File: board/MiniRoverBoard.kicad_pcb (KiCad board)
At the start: 2 copper layers, 103.4 x 66.5 mm, 49 parts, among them J1 DEBUG, Q1 NMOS, Q2 BSS138, U2 OKI, U3 Opamp_Dual, U4 LT1910, U7 ESP32-S2-DEVKITM-1U, U8 Opamp_Dual

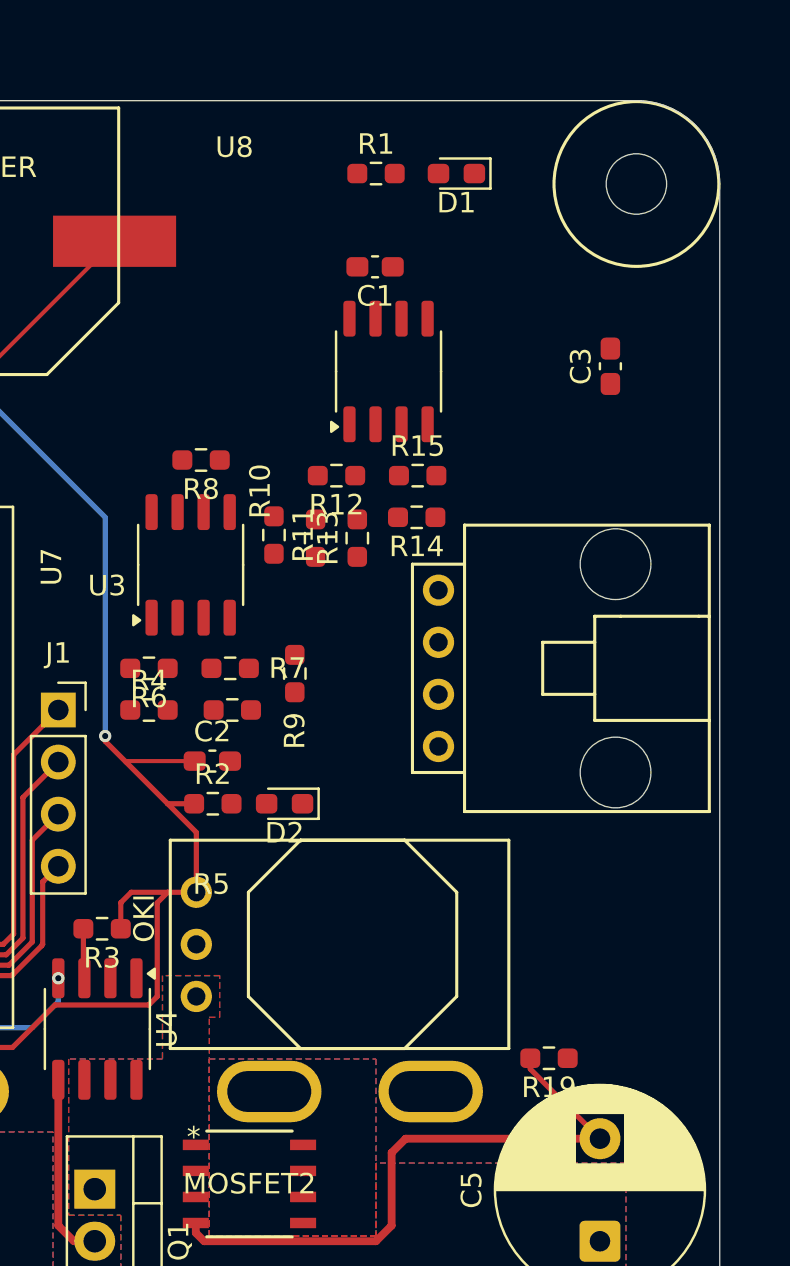
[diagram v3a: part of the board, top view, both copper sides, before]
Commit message: Add 12V trace
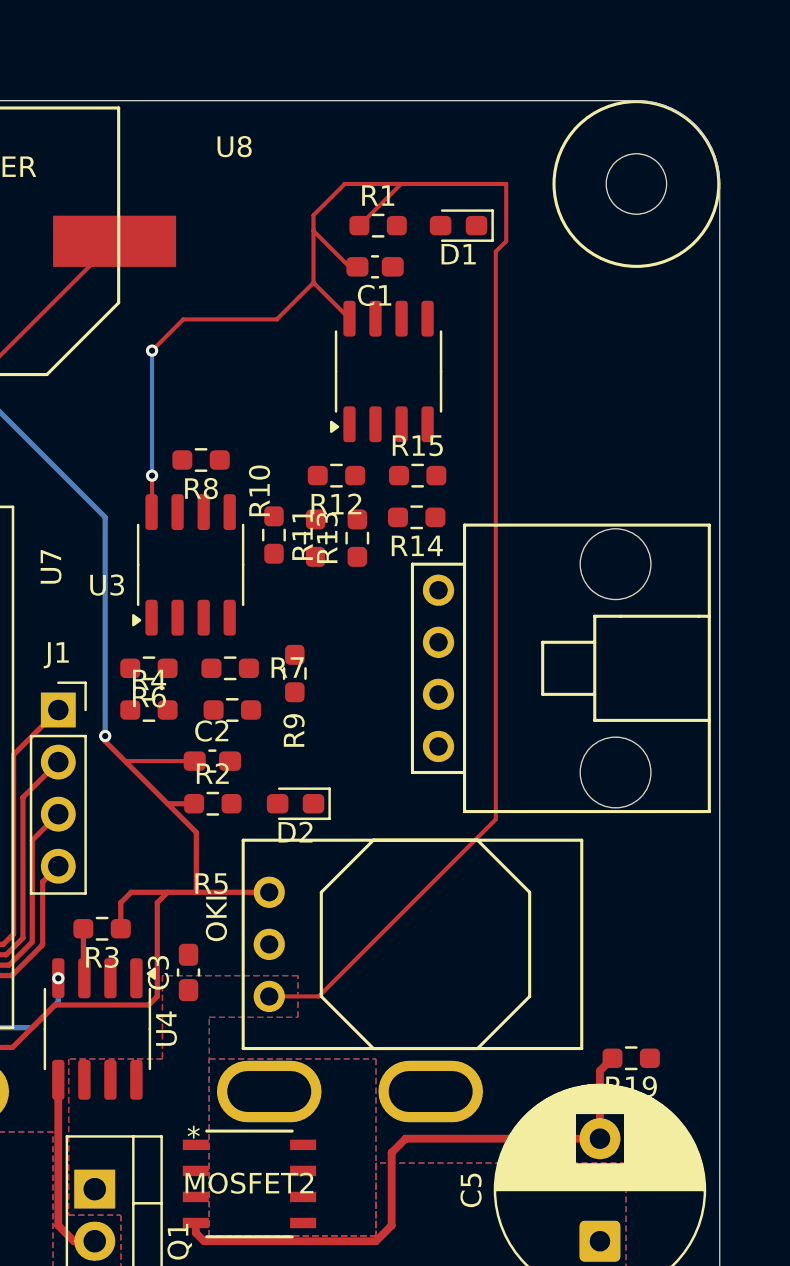
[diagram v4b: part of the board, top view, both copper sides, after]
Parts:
- moved C3 36.0 mm to (121.9, 77.3)
- moved R19 4.01 mm to (143.5, 81.5)
- moved U2 3.56 mm to (125.9, 78.5)
- moved D1 2.54 mm to (135.1, 40.9)
- moved R1 2.54 mm to (131.2, 40.9)
- moved D2 0.54 mm to (127.1, 69.1)
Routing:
- net +12V: track 0.00 -> 84.5 mm, vias 0 -> 2
- net +5V: track 192.5 -> 196.1 mm
- net Net-(MOSFET2-GATE): track 29.8 -> 28.7 mm
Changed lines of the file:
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@@
 	(footprint "LED_SMD:LED_0603_1608Metric_Pad1.05x0.95mm_HandSolder"
 		(layer "F.Cu")
-		(at 126.605 69.088 180)
+		(at 127.141 69.088 180)
 		(descr "LED SMD 0603 (1608 Metric), square (rectangular) end terminal, IPC-7351 nominal, (Body size source: http://www.tortai-tech.com/upload/download/2011102023233369053.pdf), generated with kicad-footprint-generator")
 		(tags "LED handsolder")
@@
 	(footprint "LED_SMD:LED_0603_1608Metric_Pad1.05x0.95mm_HandSolder"
 		(layer "F.Cu")
-		(at 134.987 38.354 180)
+		(at 135.0905 40.894 180)
 		(descr "LED SMD 0603 (1608 Metric), square (rectangular) end terminal, IPC-7351 nominal, (Body size source: http://www.tortai-tech.com/upload/download/2011102023233369053.pdf), generated with kicad-footprint-generator")
 		(tags "LED handsolder")
@@
 	(footprint "Capacitor_SMD:C_0603_1608Metric_Pad1.08x0.95mm_HandSolder"
 		(layer "F.Cu")
-		(at 142.494 47.752 90)
+		(at 121.92 77.3165 90)
 		(descr "Capacitor SMD 0603 (1608 Metric), square (rectangular) end terminal, IPC-7351 nominal with elongated pad for handsoldering. (Body size source: IPC-SM-782 page 76, https://www.pcb-3d.com/wordpress/wp-content/uploads/ipc-sm-782a_amendment_1_and_2.pdf), generated with kicad-footprint-generator")
 		(tags "capacitor handsolder")
@@
 	(footprint "MRDT_Devices:OKI_Horizontal"
 		(layer "F.Cu")
-		(at 122.301 78.486 90)
+		(at 125.857 78.486 90)
 		(tags "OKI")
 		(property "Reference" "U2"
@@
 	(footprint "Resistor_SMD:R_0603_1608Metric_Pad0.98x0.95mm_HandSolder"
 		(layer "F.Cu")
-		(at 139.5 81.5 180)
+		(at 143.51 81.5 180)
 		(descr "Resistor SMD 0603 (1608 Metric), square (rectangular) end terminal, IPC-7351 nominal with elongated pad for handsoldering. (Body size source: IPC-SM-782 page 72, https://www.pcb-3d.com/wordpress/wp-content/uploads/ipc-sm-782a_amendment_1_and_2.pdf), generated with kicad-footprint-generator")
 		(tags "resistor handsolder")
@@
 	(footprint "Resistor_SMD:R_0603_1608Metric_Pad0.98x0.95mm_HandSolder"
 		(layer "F.Cu")
-		(at 131.064 38.354)
+		(at 131.1675 40.894)
 		(descr "Resistor SMD 0603 (1608 Metric), square (rectangular) end terminal, IPC-7351 nominal with elongated pad for handsoldering. (Body size source: IPC-SM-782 page 72, https://www.pcb-3d.com/wordpress/wp-content/uploads/ipc-sm-782a_amendment_1_and_2.pdf), generated with kicad-footprint-generator")
 		(tags "resistor handsolder")
@@
 	)
 	(segment
+		(start 137.414 41.656)
+		(end 137.414 38.862)
+		(width 0.2)
+		(layer "F.Cu")
+		(net 2)
+	)
+	(segment
+		(start 132.287 38.862)
+		(end 130.255 40.894)
+		(width 0.2)
+		(layer "F.Cu")
+		(net 2)
+	)
+	(segment
+		(start 129.77 42.902)
+		(end 130.156 42.902)
+		(width 0.2)
+		(layer "F.Cu")
+		(net 2)
+	)
+	(segment
+		(start 132.287 38.862)
+		(end 129.54 38.862)
+		(width 0.2)
+		(layer "F.Cu")
+		(net 2)
+	)
+	(segment
+		(start 125.857 78.486)
+		(end 128.27 78.486)
+		(width 0.2)
+		(layer "F.Cu")
+		(net 2)
+	)
+	(segment
+		(start 128.016 41.148)
+		(end 128.016 43.6765)
+		(width 0.2)
+		(layer "F.Cu")
+		(net 2)
+	)
+	(segment
+		(start 121.666 45.466)
+		(end 120.142 46.99)
+		(width 0.2)
+		(layer "F.Cu")
+		(net 2)
+	)
+	(segment
+		(start 128.016 43.6765)
+		(end 126.238 45.4545)
+		(width 0.2)
+		(layer "F.Cu")
+		(net 2)
+	)
+	(segment
+		(start 128.016 40.386)
+		(end 128.016 41.148)
+		(width 0.2)
+		(layer "F.Cu")
+		(net 2)
+	)
+	(segment
+		(start 120.142 54.8405)
+		(end 120.1185 54.864)
+		(width 0.2)
+		(layer "F.Cu")
+		(net 2)
+	)
+	(segment
+		(start 137.414 38.862)
+		(end 132.287 38.862)
+		(width 0.2)
+		(layer "F.Cu")
+		(net 2)
+	)
+	(segment
+		(start 128.27 78.486)
+		(end 136.906 69.85)
+		(width 0.2)
+		(layer "F.Cu")
+		(net 2)
+	)
+	(segment
+		(start 120.142 53.086)
+		(end 120.142 54.8405)
+		(width 0.2)
+		(layer "F.Cu")
+		(net 2)
+	)
+	(segment
+		(start 126.238 45.4545)
+		(end 126.238 45.466)
+		(width 0.2)
+		(layer "F.Cu")
+		(net 2)
+	)
+	(segment
+		(start 126.238 45.466)
+		(end 121.666 45.466)
+		(width 0.2)
+		(layer "F.Cu")
+		(net 2)
+	)
+	(segment
+		(start 128.016 43.6765)
+		(end 129.7705 45.431)
+		(width 0.2)
+		(layer "F.Cu")
+		(net 2)
+	)
+	(segment
+		(start 128.016 41.148)
+		(end 129.77 42.902)
+		(width 0.2)
+		(layer "F.Cu")
+		(net 2)
+	)
+	(segment
+		(start 136.906 69.85)
+		(end 136.906 42.164)
+		(width 0.2)
+		(layer "F.Cu")
+		(net 2)
+	)
+	(segment
+		(start 136.906 42.164)
+		(end 137.414 41.656)
+		(width 0.2)
+		(layer "F.Cu")
+		(net 2)
+	)
+	(segment
+		(start 129.54 38.862)
+		(end 128.016 40.386)
+		(width 0.2)
+		(layer "F.Cu")
+		(net 2)
+	)
+	(via
+		(at 120.142 53.086)
+		(size 0.6)
+		(drill 0.3)
+		(layers "F.Cu" "B.Cu")
+		(net 2)
+	)
+	(via
+		(at 120.142 46.99)
+		(size 0.6)
+		(drill 0.3)
+		(layers "F.Cu" "B.Cu")
+		(net 2)
+	)
+	(segment
+		(start 120.142 46.99)
+		(end 120.142 53.086)
+		(width 0.2)
+		(layer "B.Cu")
+		(net 2)
+	)
+	(segment
 		(start 61.394 53.774)
 		(end 61.394 47.649)
@@
 	)
 	(segment
+		(start 122.301 73.406)
+		(end 125.857 73.406)
+		(width 0.254)
+		(layer "F.Cu")
+		(net 3)
+	)
+	(segment
 		(start 93.98 87.63)
 		(end 95.758 87.63)
@@
 	)
 	(segment
-		(start 138.5875 82.0255)
-		(end 141.986 85.424)
-		(width 0.254)
-		(layer "F.Cu")
-		(net 62)
-	)
-	(segment
 		(start 122.682 90.424)
 		(end 131.064 90.424)
@@
 	)
 	(segment
-		(start 132.508 85.424)
-		(end 141.986 85.424)
+		(start 141.986 82.1115)
+		(end 142.5975 81.5)
 		(width 0.381)
 		(layer "F.Cu")
@@
 	)
 	(segment
-		(start 138.5875 81.5)
-		(end 138.5875 82.0255)
-		(width 0.254)
+		(start 132.508 85.424)
+		(end 141.986 85.424)
+		(width 0.381)
 		(layer "F.Cu")
 		(net 62)
@@
 	)
 	(segment
+		(start 141.986 85.424)
+		(end 141.986 82.1115)
+		(width 0.381)
+		(layer "F.Cu")
+		(net 62)
+	)
+	(segment
 		(start 108.4856 86.487)
 		(end 109.2962 86.487)
@@
 		(polygon
 			(pts
-				(xy 122.936 79.502) (xy 123.444 79.502) (xy 123.444 77.47) (xy 120.65 77.47) (xy 120.65 81.534)
+				(xy 122.936 79.502) (xy 127.254 79.502) (xy 127.254 77.47) (xy 120.65 77.47) (xy 120.65 81.534)
 				(xy 116.078 81.534) (xy 116.078 89.154) (xy 118.618 89.154) (xy 118.623134 97.791444) (xy 139.446 97.79)
 				(xy 139.446 93.218) (xy 143.256 93.218) (xy 143.256 86.614) (xy 131.064 86.614) (xy 131.064 90.17)

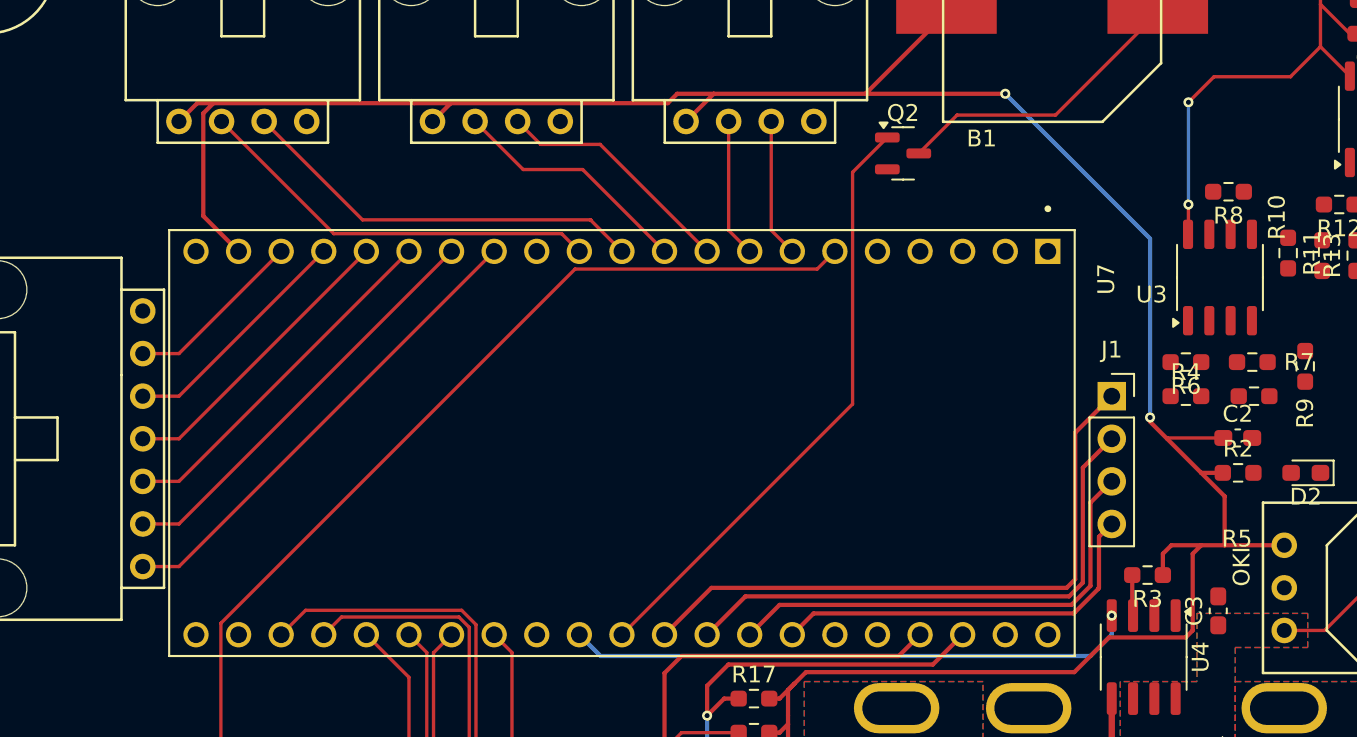
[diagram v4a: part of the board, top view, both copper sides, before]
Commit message: Add TFT Backlight trace
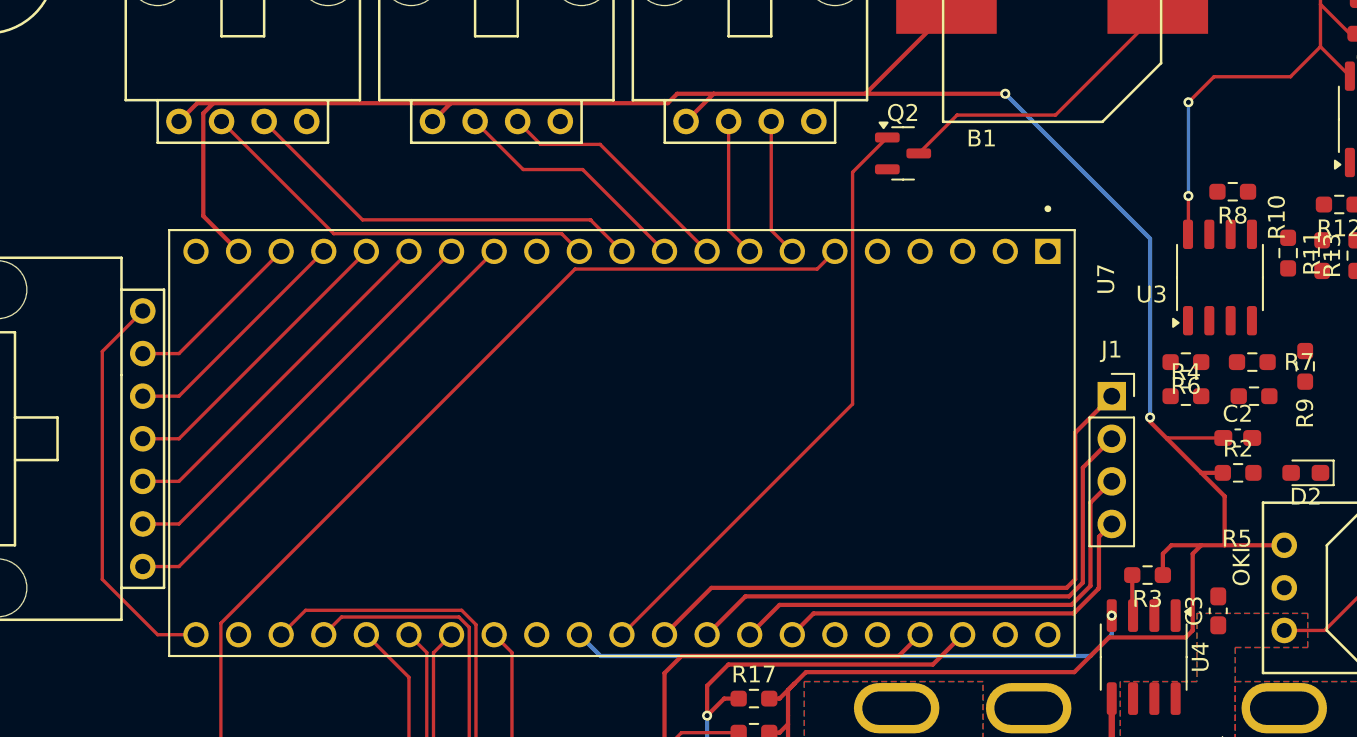
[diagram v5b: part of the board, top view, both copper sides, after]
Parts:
- moved R8 0.25 mm to (122.8, 52.3)
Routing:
- net TFT_Backlight: track 0.00 -> 24.0 mm
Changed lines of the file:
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@@
 	(footprint "Resistor_SMD:R_0603_1608Metric_Pad0.98x0.95mm_HandSolder"
 		(layer "F.Cu")
-		(at 122.5315 52.324 180)
+		(at 122.7855 52.324 180)
 		(descr "Resistor SMD 0603 (1608 Metric), square (rectangular) end terminal, IPC-7351 nominal with elongated pad for handsoldering. (Body size source: IPC-SM-782 page 72, https://www.pcb-3d.com/wordpress/wp-content/uploads/ipc-sm-782a_amendment_1_and_2.pdf), generated with kicad-footprint-generator")
 		(tags "resistor handsolder")
@@
 	)
 	(segment
+		(start 120.142 54.8405)
+		(end 120.1185 54.864)
+		(width 0.2)
+		(layer "F.Cu")
+		(net 2)
+	)
+	(segment
 		(start 132.287 38.862)
 		(end 129.54 38.862)
@@
 	)
 	(segment
-		(start 120.142 54.8405)
-		(end 120.1185 54.864)
+		(start 120.142 52.578)
+		(end 120.142 54.8405)
 		(width 0.2)
 		(layer "F.Cu")
@@
 	)
 	(segment
-		(start 120.142 53.086)
-		(end 120.142 54.8405)
-		(width 0.2)
-		(layer "F.Cu")
-		(net 2)
-	)
-	(segment
 		(start 126.238 45.4545)
 		(end 126.238 45.466)
@@
 	)
 	(via
-		(at 120.142 53.086)
+		(at 120.142 52.578)
 		(size 0.6)
 		(drill 0.3)
@@
 	(segment
 		(start 120.142 46.99)
-		(end 120.142 53.086)
+		(end 120.142 52.578)
 		(width 0.2)
 		(layer "B.Cu")
@@
 	)
 	(segment
+		(start 58.674 78.74)
+		(end 55.372 75.438)
+		(width 0.2)
+		(layer "F.Cu")
+		(net 20)
+	)
+	(segment
+		(start 55.372 75.438)
+		(end 55.372 61.849)
+		(width 0.2)
+		(layer "F.Cu")
+		(net 20)
+	)
+	(segment
+		(start 60.96 78.74)
+		(end 58.674 78.74)
+		(width 0.2)
+		(layer "F.Cu")
+		(net 20)
+	)
+	(segment
+		(start 55.372 61.849)
+		(end 57.785 59.436)
+		(width 0.2)
+		(layer "F.Cu")
+		(net 20)
+	)
+	(segment

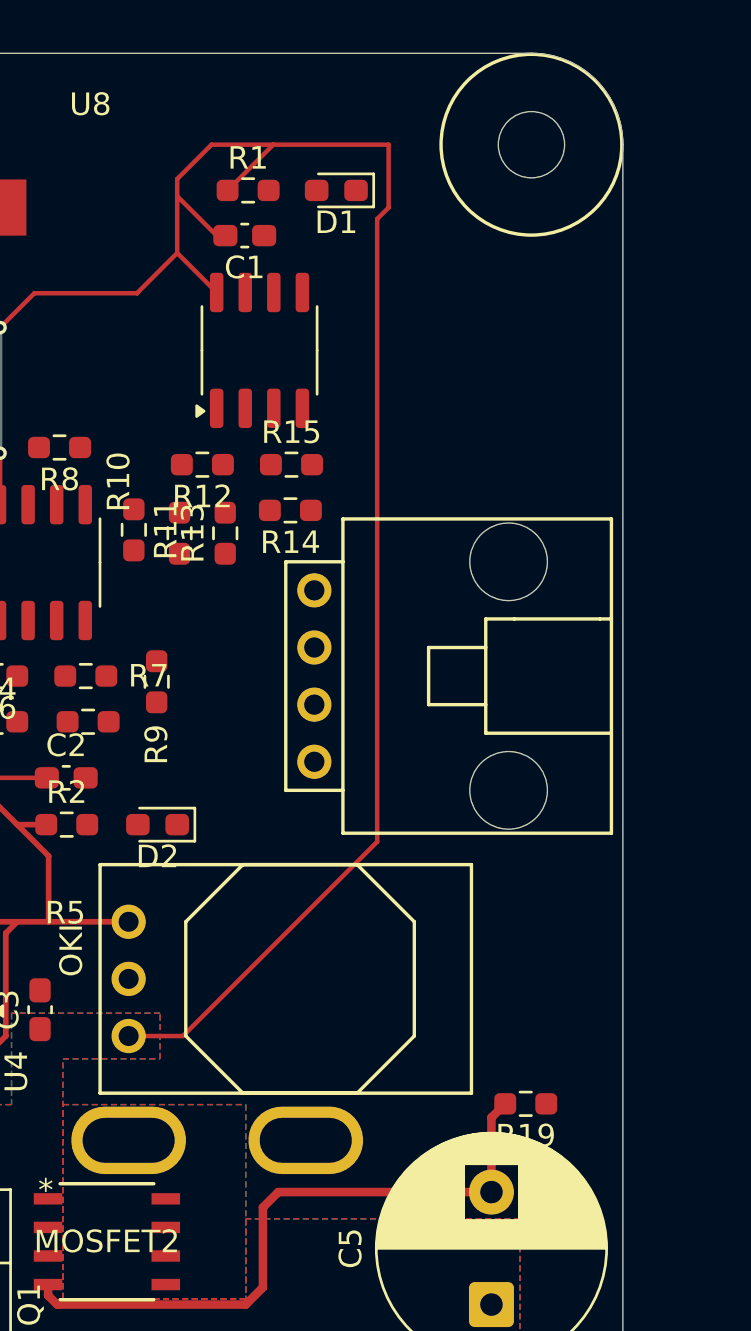
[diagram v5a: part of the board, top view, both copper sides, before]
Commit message: Move 12 volt Oki Components next to Oki
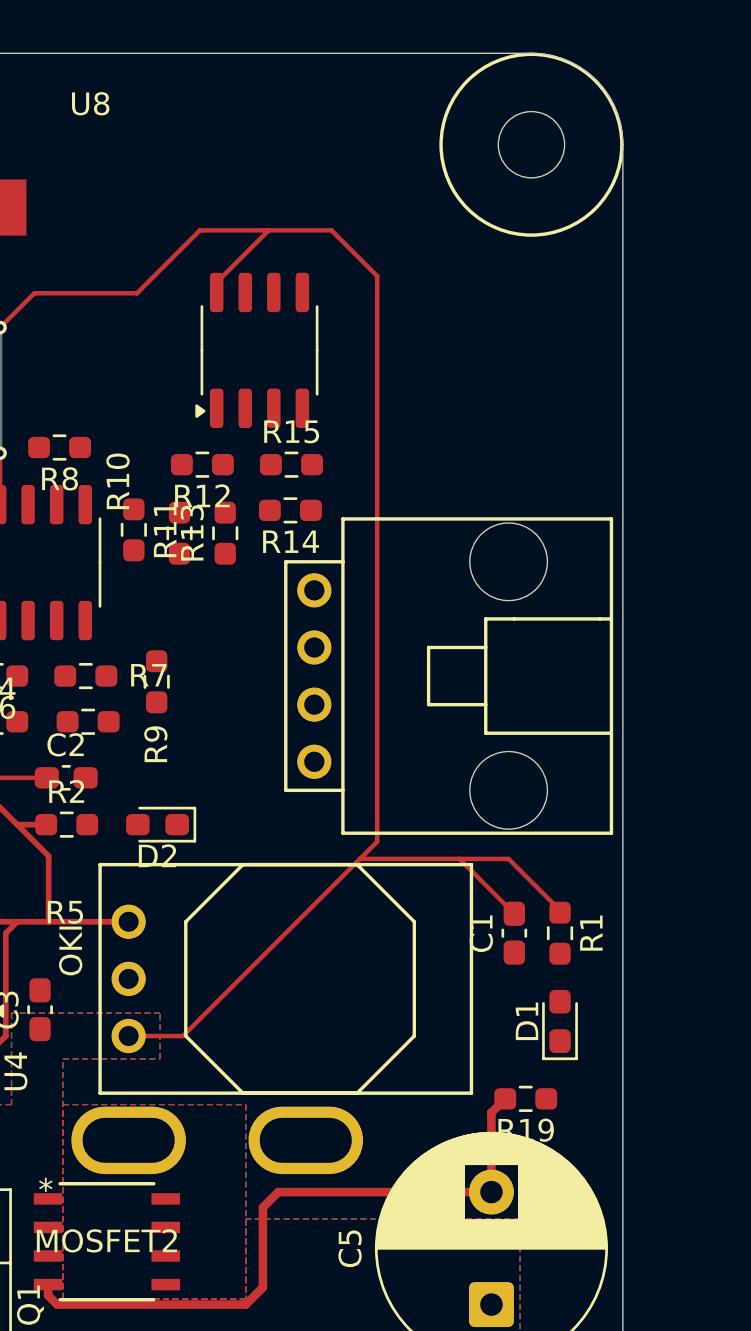
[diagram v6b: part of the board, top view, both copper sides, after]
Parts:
- moved D1 38.3 mm to (145.0, 77.8), turned to 90 degrees
- moved R1 35.8 mm to (145.0, 73.9), turned to -90 degrees
- moved C1 33.2 mm to (143.0, 73.9), turned to 90 degrees
- moved R19 0.22 mm to (143.5, 81.3)
